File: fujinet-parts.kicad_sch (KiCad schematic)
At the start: 1 part

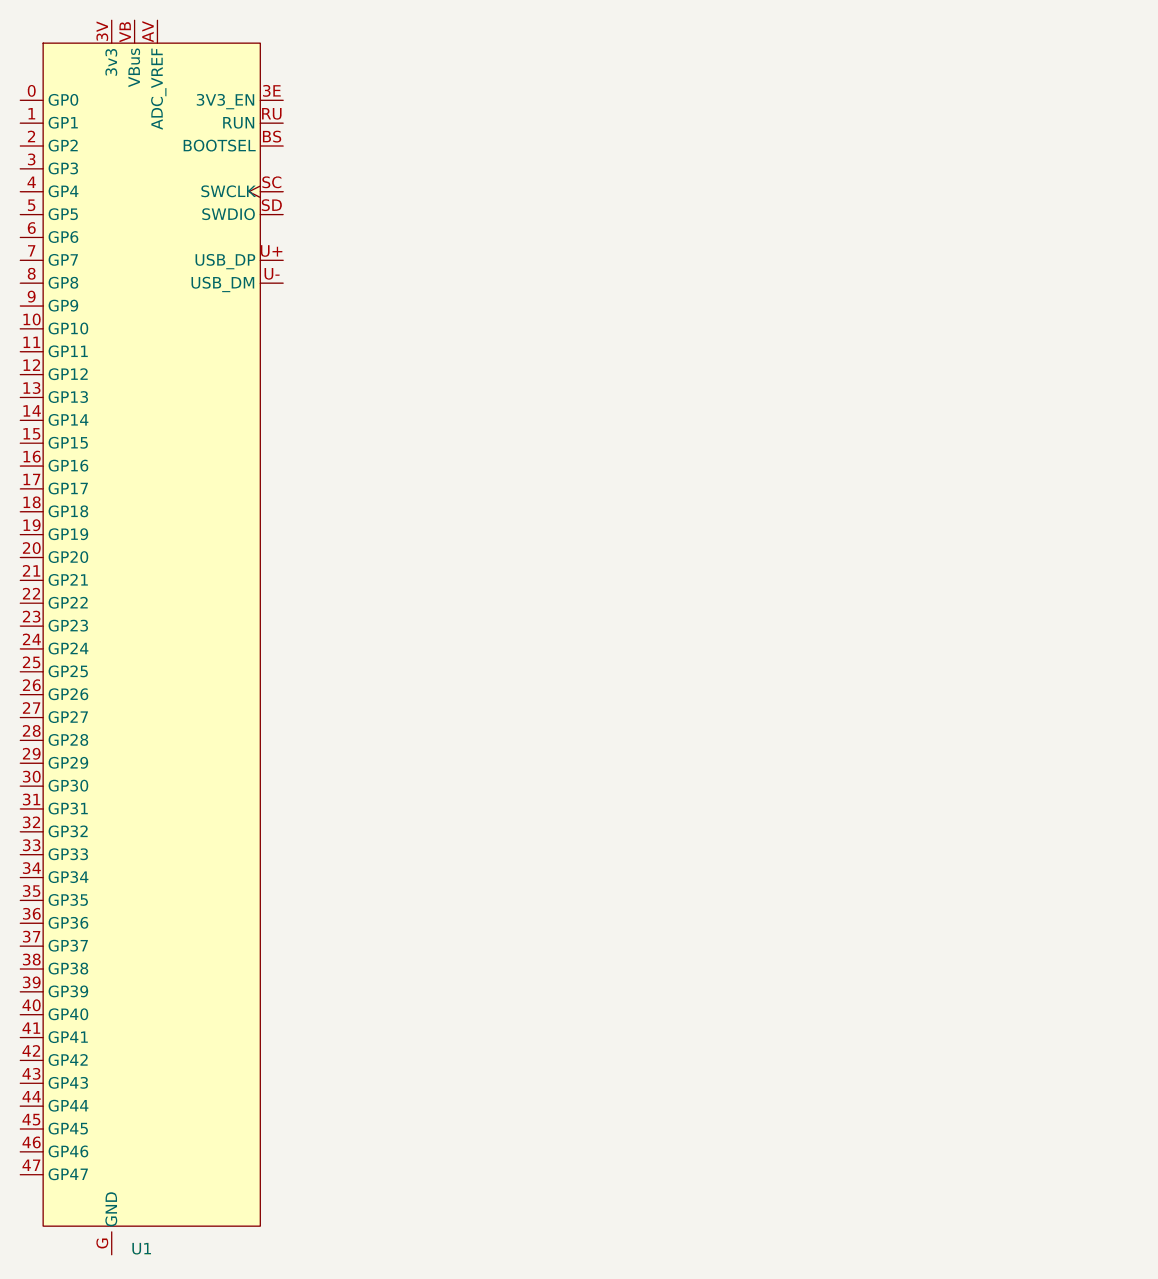
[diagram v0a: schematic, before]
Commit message: ESP32-S3-CAM
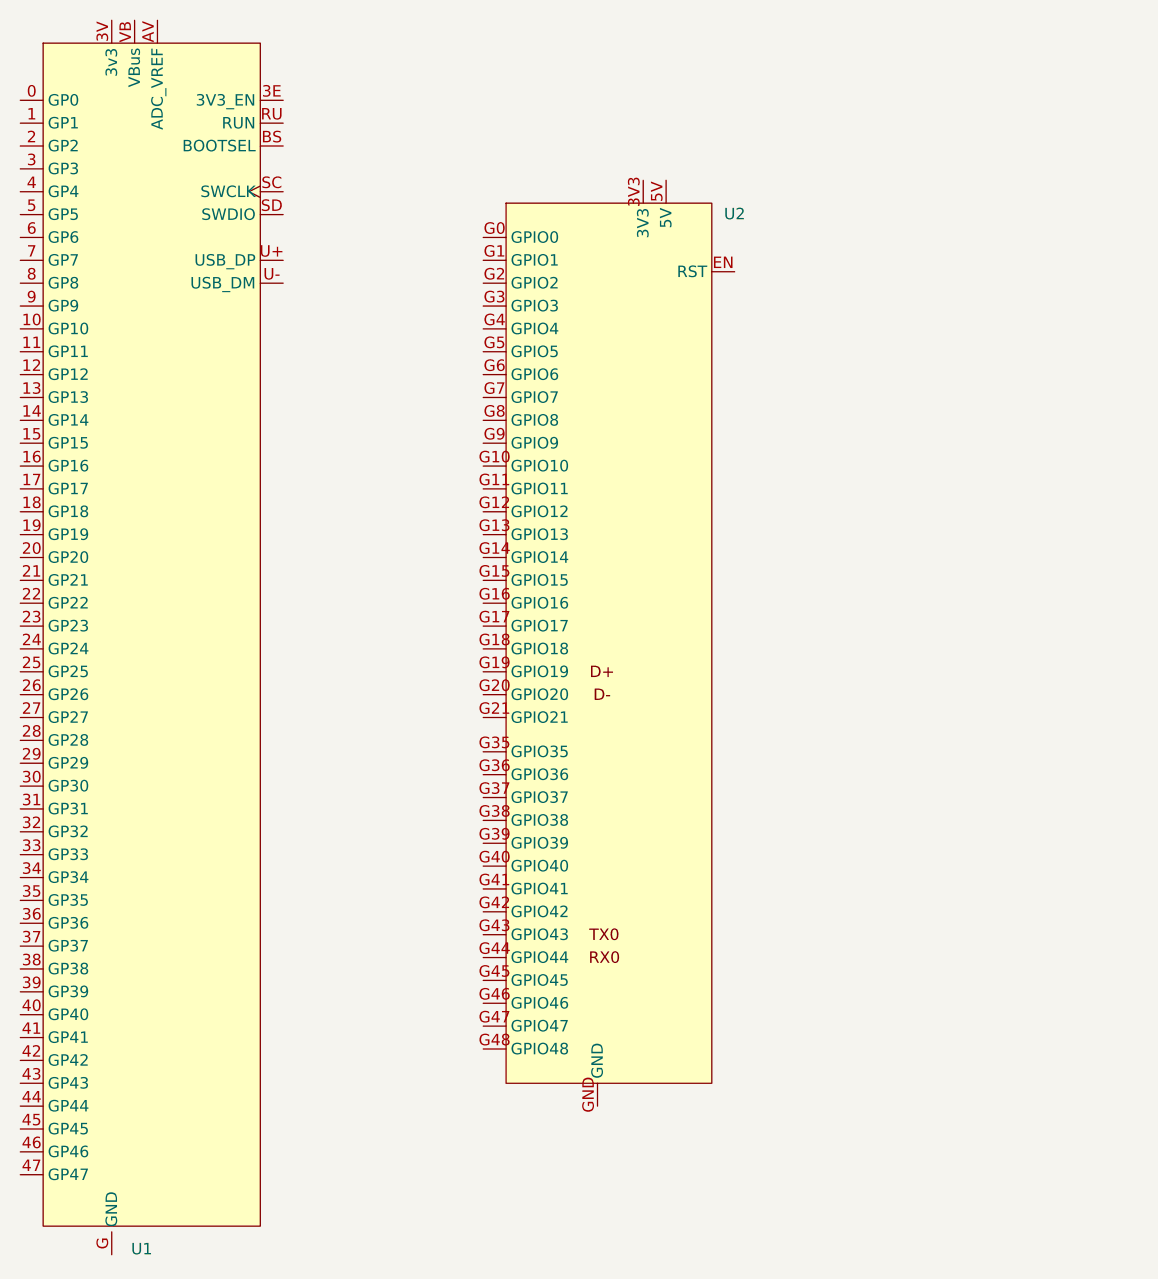
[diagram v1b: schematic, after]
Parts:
- added U2: ~, FujiNet:ESP32-S3-CAM, symbol FujiNet:ESP32-S3-CAM
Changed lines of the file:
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@@
+		)
+	)
+	(symbol
+		(lib_id "FujiNet:ESP32-S3-CAM")
+		(at 83.82 38.735 0)
+		(unit 1)
+		(exclude_from_sim no)
+		(in_bom yes)
+		(on_board yes)
+		(dnp no)
+		(fields_autoplaced yes)
+		(property "Reference" "U2"
+			(at 99.06 43.7448 0)
+			(effects
+				(font
+					(size 1.27 1.27)
+				)
+			)
+		)
+		(property "Value" "~"
+			(at 99.06 46.2848 0)
+			(effects
+				(font
+					(size 1.27 1.27)
+				)
+			)
+		)
+		(property "Footprint" "FujiNet:ESP32-S3-CAM"
+			(at 83.82 38.735 0)
+			(effects
+				(font
+					(size 1.27 1.27)
+				)
+				(hide yes)
+			)
+		)
+		(property "Datasheet" "https://www.amazon.com/dp/B0F4DKTBR9?th=1"
+			(at 83.82 38.735 0)
+			(effects
+				(font
+					(size 1.27 1.27)
+				)
+				(hide yes)
+			)
+		)
+		(property "Description" "ESP32-S3-WROOM development board"
+			(at 83.82 38.735 0)
+			(effects
+				(font
+					(size 1.27 1.27)
+				)
+				(hide yes)
+			)
+		)
+		(pin "G19"
+		)
+		(pin "G20"
+		)
+		(pin "G5"
+		)
+		(pin "G11"
+		)
+		(pin "G12"
+		)
+		(pin "G13"
+		)
+		(pin "G14"
+		)
+		(pin "G15"
+		)
+		(pin "G16"
+		)
+		(pin "G8"
+		)
+		(pin "G9"
+		)
+		(pin "G10"
+		)
+		(pin "G17"
+		)
+		(pin "G18"
+		)
+		(pin "G21"
+		)
+		(pin "G35"
+		)
+		(pin "G36"
+		)
+		(pin "G37"
+		)
+		(pin "G38"
+		)
+		(pin "G39"
+		)
+		(pin "G40"
+		)
+		(pin "G41"
+		)
+		(pin "G42"
+		)
+		(pin "G43"
+		)
+		(pin "G44"
+		)
+		(pin "G45"
+		)
+		(pin "G46"
+		)
+		(pin "G47"
+		)
+		(pin "G48"
+		)
+		(pin "GND"
+		)
+		(pin "3V3"
+		)
+		(pin "5V"
+		)
+		(pin "EN"
+		)
+		(pin "G0"
+		)
+		(pin "G1"
+		)
+		(pin "G3"
+		)
+		(pin "G2"
+		)
+		(pin "G7"
+		)
+		(pin "G6"
+		)
+		(pin "G4"
+		)
+		(instances
+			(project ""
+				(path "/88ea2842-8e8d-4bde-98e3-2cb923ce1bc7"
+					(reference "U2")
+					(unit 1)
+				)
+			)
 		)
 	)

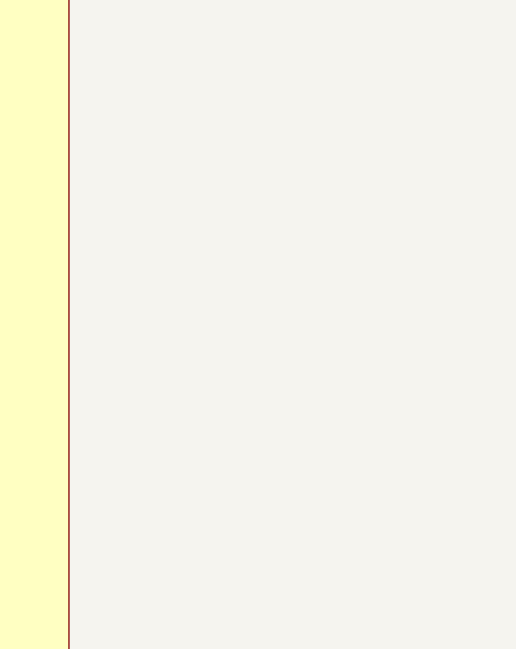
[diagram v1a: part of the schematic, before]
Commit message: Link 98357A symbol and footprint
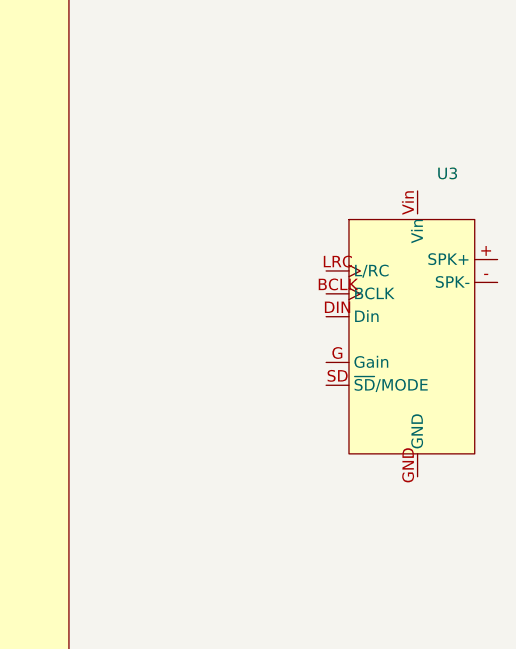
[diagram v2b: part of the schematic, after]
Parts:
- added U3: ~, FujiNet:MAX98357A_i2c_Breakout, symbol FujiNet:MAX98357a_Breakout
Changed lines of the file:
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@@
+	)
+	(symbol
+		(lib_id "FujiNet:MAX98357a_Breakout")
+		(at 135.255 70.485 0)
+		(unit 1)
+		(exclude_from_sim no)
+		(in_bom yes)
+		(on_board yes)
+		(dnp no)
+		(fields_autoplaced yes)
+		(property "Reference" "U3"
+			(at 137.3983 71.12 0)
+			(effects
+				(font
+					(size 1.27 1.27)
+				)
+				(justify left)
+			)
+		)
+		(property "Value" "~"
+			(at 137.3983 73.66 0)
+			(effects
+				(font
+					(size 1.27 1.27)
+				)
+				(justify left)
+			)
+		)
+		(property "Footprint" "FujiNet:MAX98357A_i2c_Breakout"
+			(at 135.255 70.485 0)
+			(effects
+				(font
+					(size 1.27 1.27)
+				)
+				(hide yes)
+			)
+		)
+		(property "Datasheet" "https://learn.adafruit.com/adafruit-max98357-i2s-class-d-mono-amp?view=all"
+			(at 135.255 70.485 0)
+			(effects
+				(font
+					(size 1.27 1.27)
+				)
+				(hide yes)
+			)
+		)
+		(property "Description" "Breakout board for the i2s interface to MAX98327A amplifier. Various copies exist on Amazon, etc, but the measurements are from Adafruit, which seem to eyeball out."
+			(at 135.255 70.485 0)
+			(effects
+				(font
+					(size 1.27 1.27)
+				)
+				(hide yes)
+			)
+		)
+		(pin "+"
+		)
+		(pin "-"
+		)
+		(pin "G"
+		)
+		(pin "DIN"
+		)
+		(pin "LRC"
+		)
+		(pin "BCLK"
+		)
+		(pin "SD"
+		)
+		(pin "GND"
+		)
+		(pin "Vin"
+		)
+		(instances
+			(project ""
+				(path "/88ea2842-8e8d-4bde-98e3-2cb923ce1bc7"
+					(reference "U3")
+					(unit 1)
+				)
+			)
+		)
 	)
 	(symbol
